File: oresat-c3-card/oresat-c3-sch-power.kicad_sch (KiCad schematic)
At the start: 68 parts, among them U31 LP2985AIM5-3.3, U34 TPS259621DDA, U35 TPS259620DDA, U36 LTC3624-5, U38 LP2985AIM5-3.3, U6 LTC3624-5

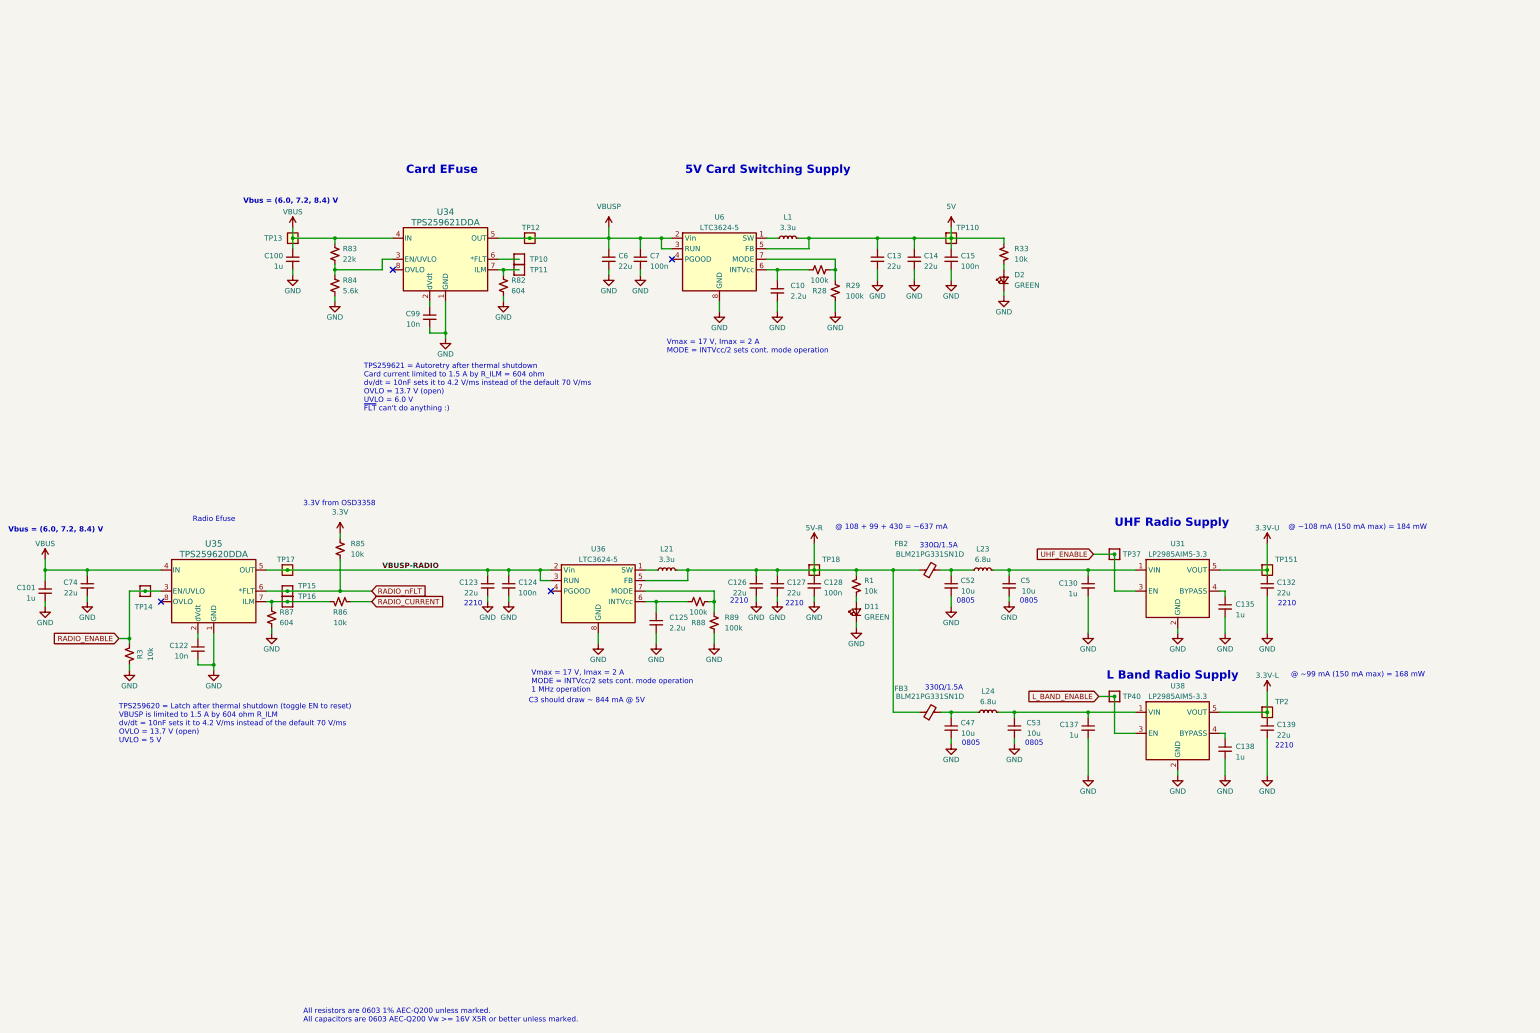
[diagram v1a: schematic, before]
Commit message: schematic changes following design review
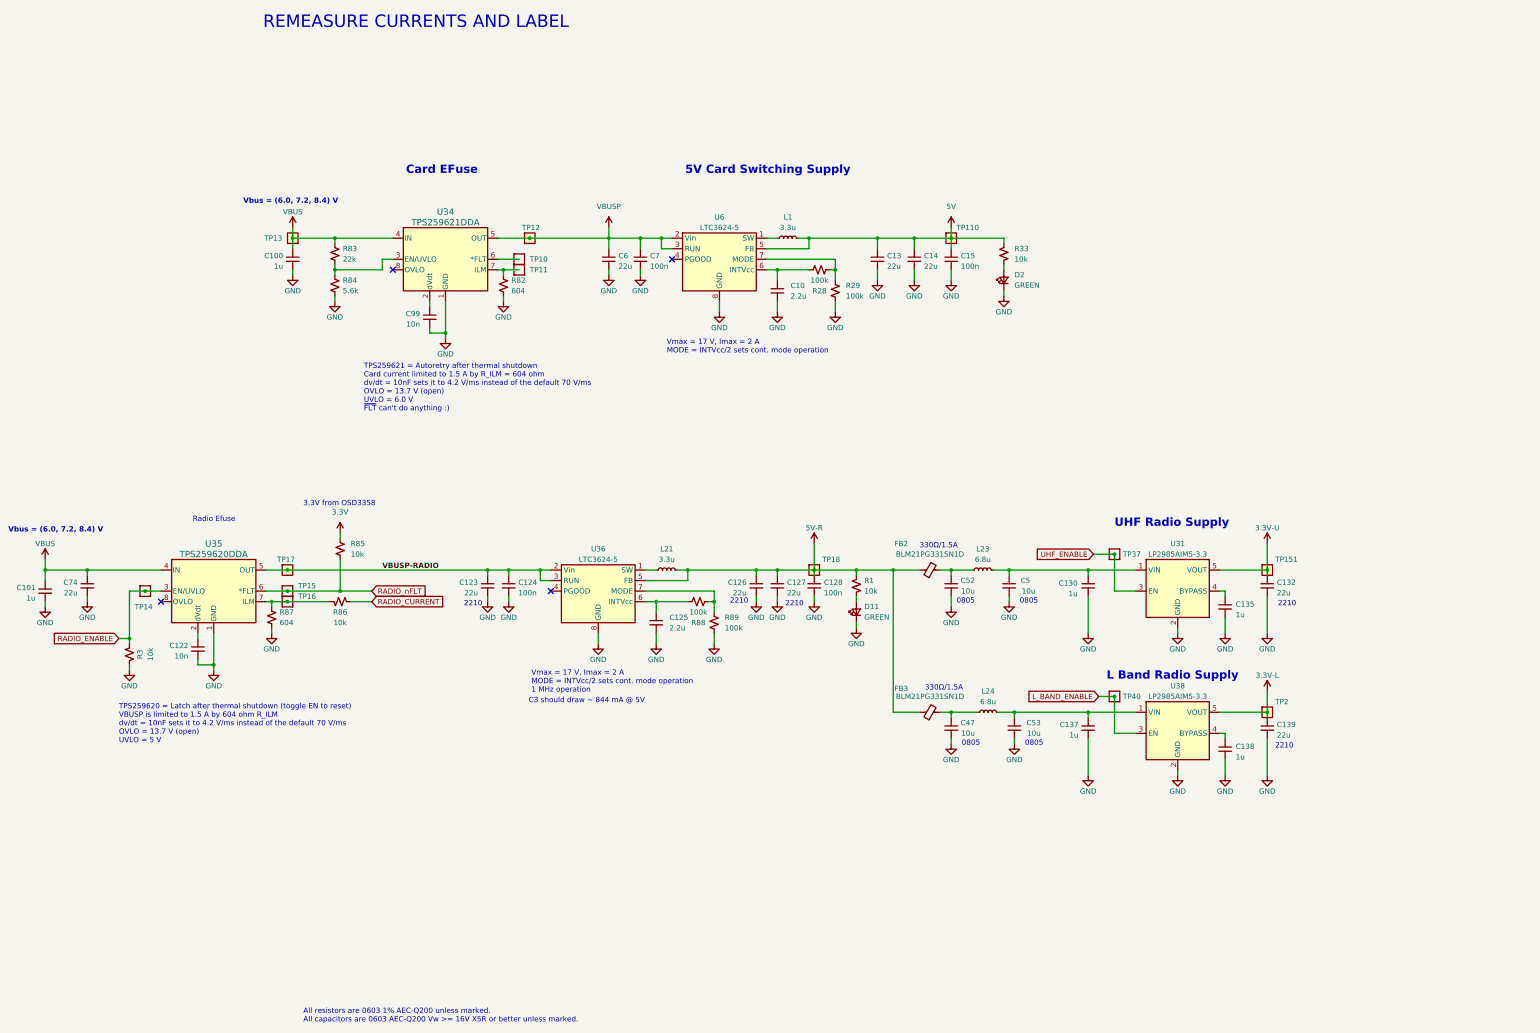
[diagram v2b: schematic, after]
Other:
- note added: "REMEASURE CURRENTS AND LABEL"
- note removed: "@ 108 + 99 + 430 = ~637 mA"
- note removed: "@ ~108 mA (150 mA max) = 184 mW"
- note removed: "@ ~99 mA (150 mA max) = 168 mW"
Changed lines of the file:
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@@
 		(company "Portland State Aerospace Society")
 	)
+	(text "REMEASURE CURRENTS AND LABEL"
+		(exclude_from_sim no)
+		(at 145.288 20.32 0)
+		(effects
+			(font
+				(size 3 3)
+			)
+		)
+	)
 	(text "330Ω/1.5A"
 		(exclude_from_sim no)
 		(at 266.7 147.32 0)
-		(effects
-			(font
-				(size 1.27 1.27)
-			)
-			(justify left bottom)
-		)
-	)
-	(text "@ ~99 mA (150 mA max) = 168 mW"
-		(exclude_from_sim no)
-		(at 356.235 178.435 0)
 		(effects
 			(font
@@
 		)
 	)
-	(text "@ 108 + 99 + 430 = ~637 mA"
-		(exclude_from_sim no)
-		(at 246.38 142.875 0)
-		(effects
-			(font
-				(size 1.27 1.27)
-			)
-			(justify left bottom)
-		)
-	)
 	(text "2210"
 		(exclude_from_sim no)
@@
 		(effects
 			(font
-				(size 1.27 1.27)
-			)
-			(justify left bottom)
-		)
-	)
-	(text "@ ~108 mA (150 mA max) = 184 mW"
-		(exclude_from_sim no)
-		(at 355.6 142.875 0)
-		(effects
-			(font

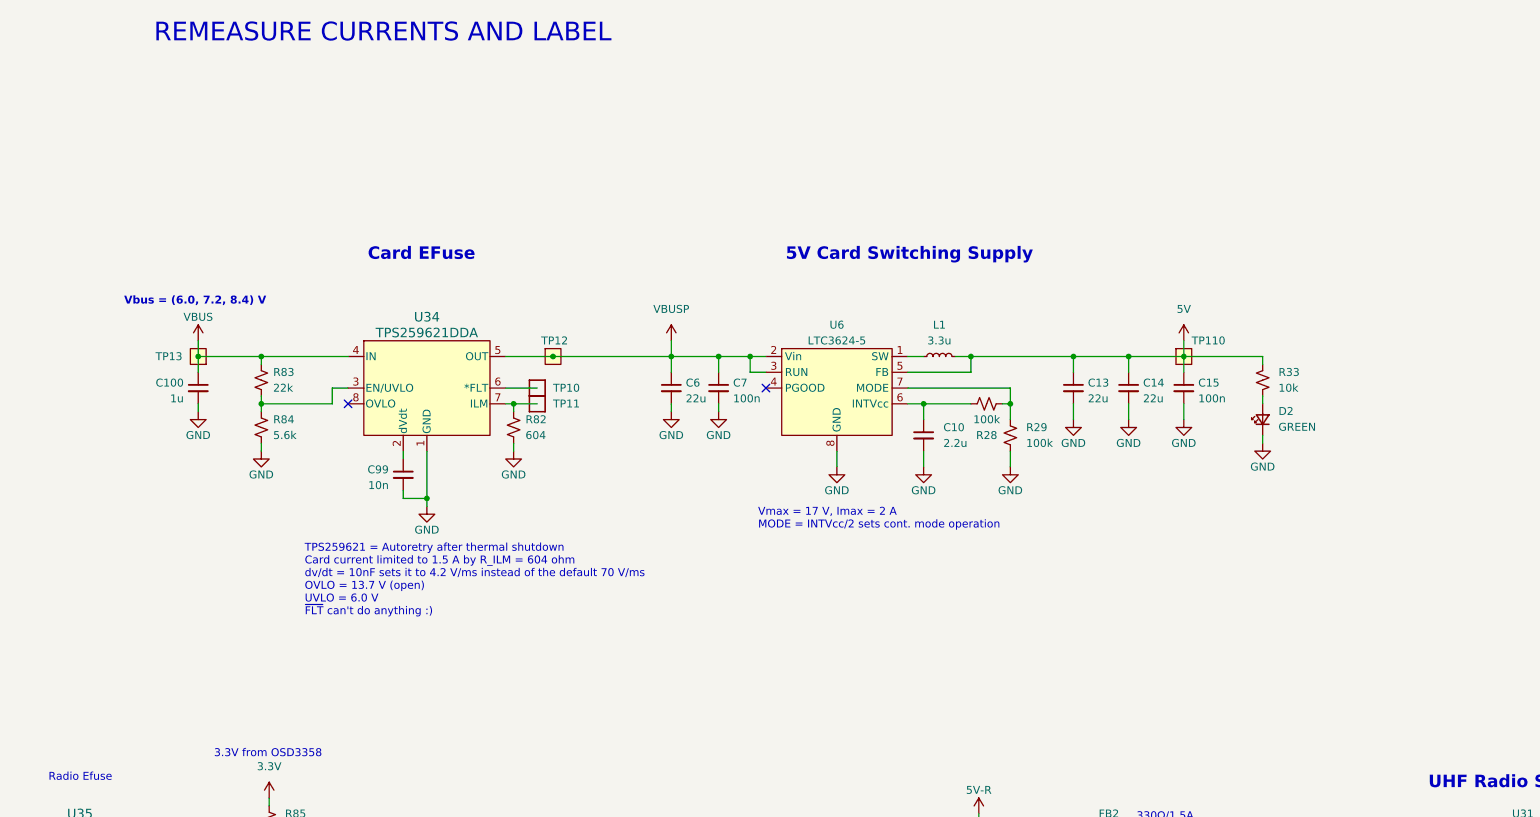
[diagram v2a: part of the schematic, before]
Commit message: Additional C3 design review changes and routing progress
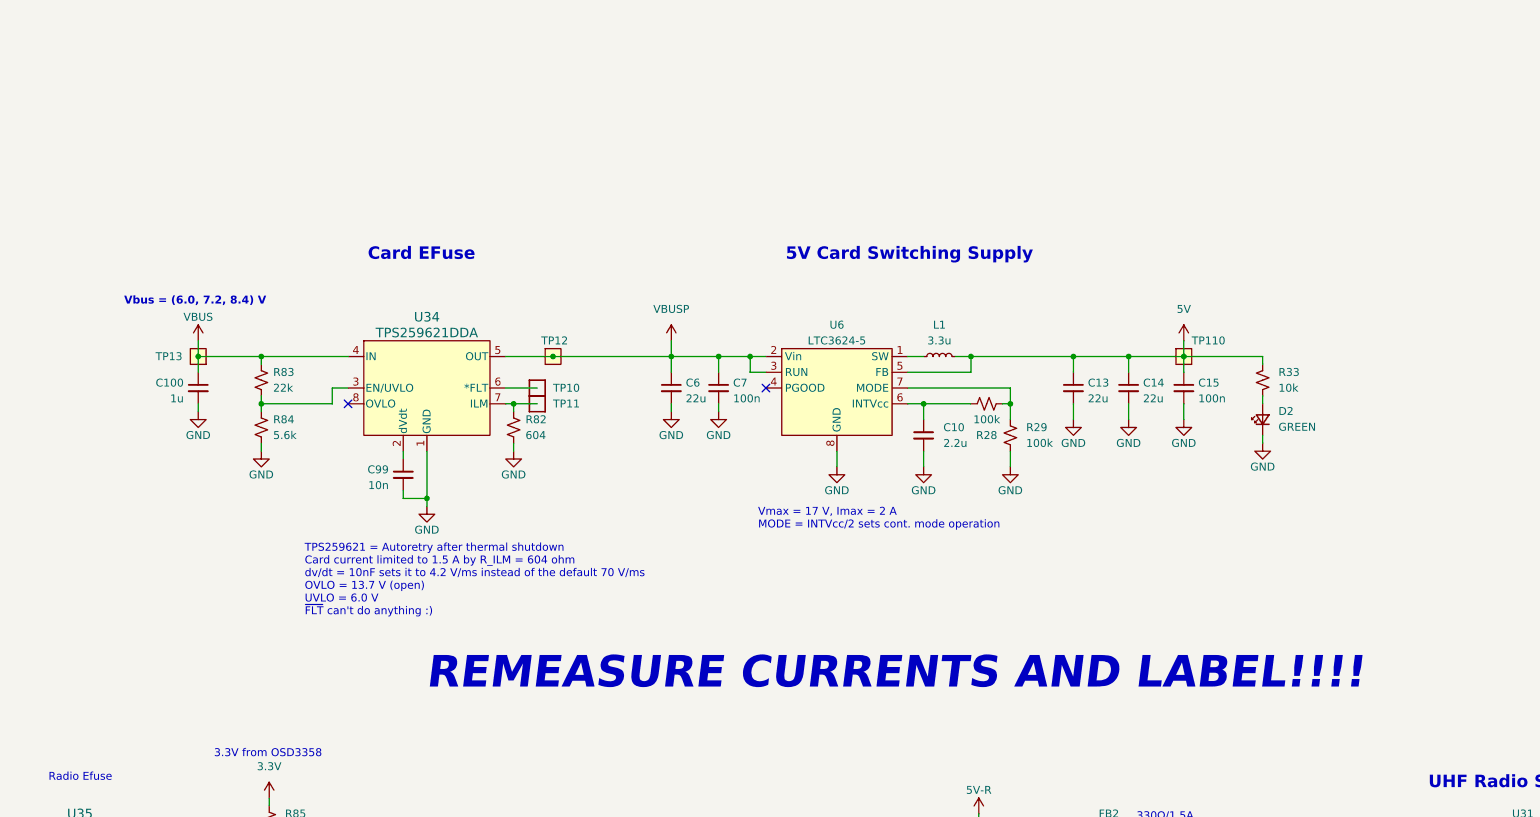
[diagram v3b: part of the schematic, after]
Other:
- note added: "REMEASURE CURRENTS AND LABEL!!!!"
- note removed: "REMEASURE CURRENTS AND LABEL"
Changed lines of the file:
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@@
 		(company "Portland State Aerospace Society")
 	)
-	(text "REMEASURE CURRENTS AND LABEL"
+	(text "REMEASURE CURRENTS AND LABEL!!!!"
 		(exclude_from_sim no)
-		(at 145.288 20.32 0)
+		(at 227.838 123.444 0)
 		(effects
 			(font
-				(size 3 3)
+				(face "KiCad Font")
+				(size 5.08 5.08)
+				(thickness 0.6)
+				(bold yes)
+				(italic yes)
+				(color 255 0 11 1)
 			)
 		)

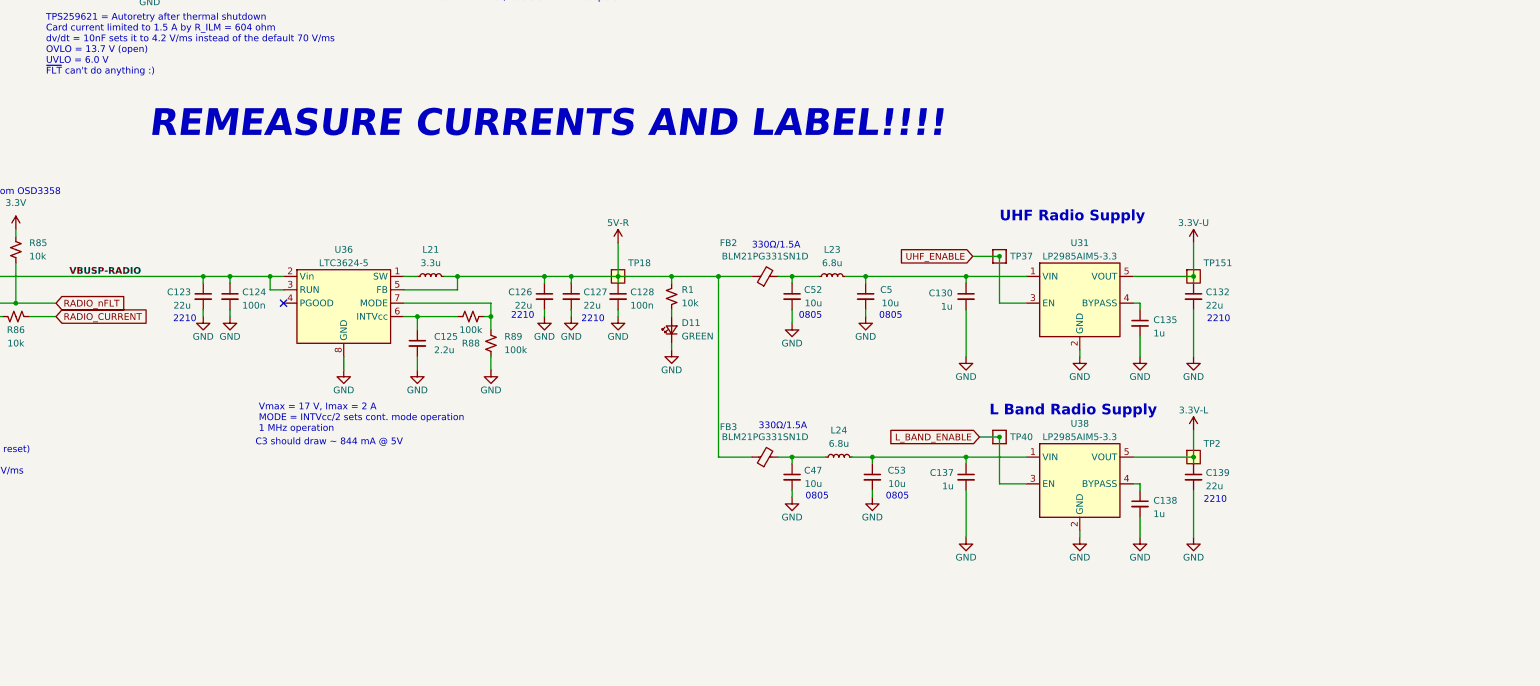
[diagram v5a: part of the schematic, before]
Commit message: Design review on C3 v7.0
Glenn and Andrew did a design review. Removed fiducials on back of board. Lots of schematic fixes, including
direction connection of TCXOs to AT86s, corrected LPF of CLKO from AT86 to the synth reference, fixed drive
levels both QPC switches in UHF radio, confirmed QPC directions, and some minor polishing.
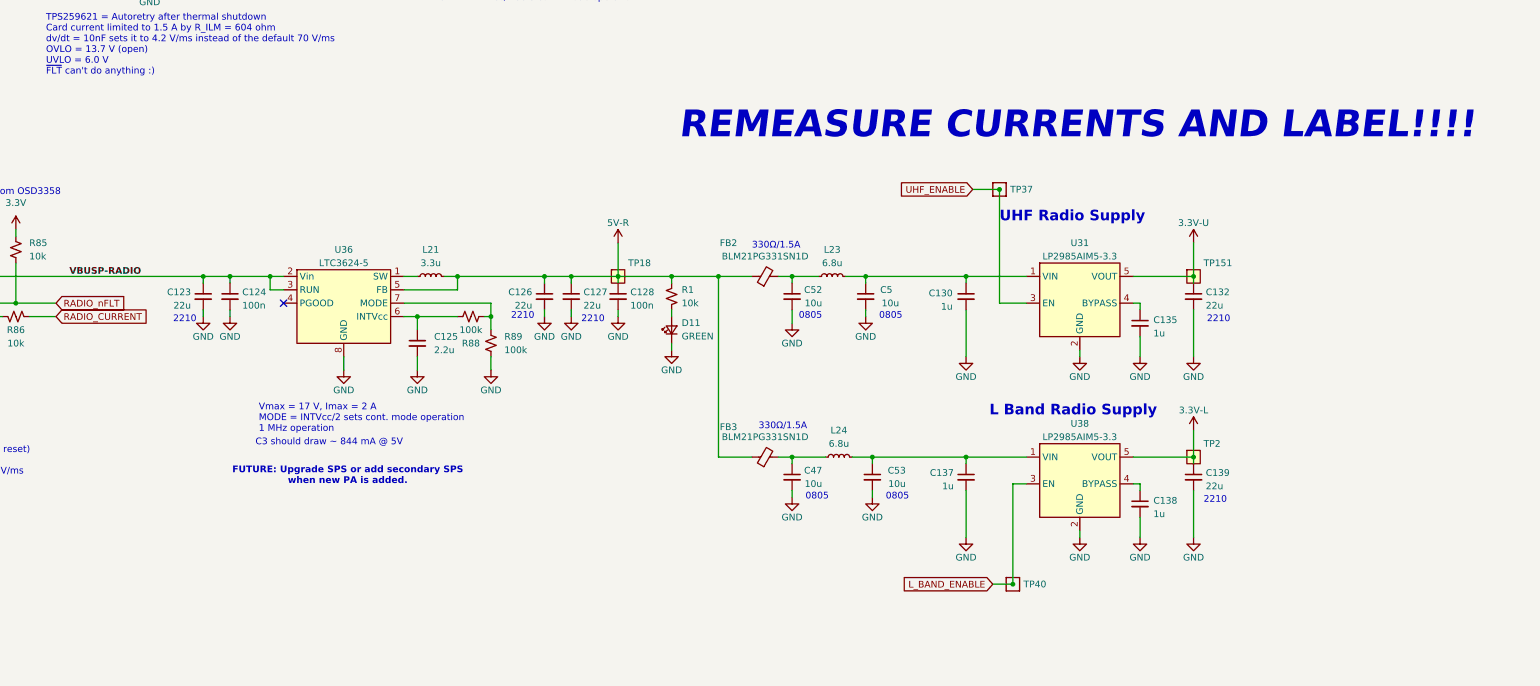
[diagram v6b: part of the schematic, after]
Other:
- note added: "FUTURE: Upgrade SPS or add secondary SPS when new PA is added."
- moved on the sheet: TP37, TP40
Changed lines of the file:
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@@
 	(text "REMEASURE CURRENTS AND LABEL!!!!"
 		(exclude_from_sim no)
-		(at 227.838 123.444 0)
+		(at 328.422 123.698 0)
 		(effects
 			(font
@@
 		)
 	)
+	(text "FUTURE: Upgrade SPS or add secondary SPS\nwhen new PA is added."
+		(exclude_from_sim no)
+		(at 189.992 190.246 0)
+		(effects
+			(font
+				(size 1.27 1.27)
+				(thickness 0.254)
+				(bold yes)
+			)
+		)
+	)
 	(text "330Ω/1.5A"
 		(exclude_from_sim no)
@@
 	)
 	(junction
-		(at 313.69 182.88)
+		(at 316.23 210.82)
 		(diameter 0)
 		(color 0 0 0 0)
@@
 	)
 	(junction
-		(at 313.69 148.59)
+		(at 313.69 135.89)
 		(diameter 0)
 		(color 0 0 0 0)
@@
 	(wire
 		(pts
-			(xy 309.88 182.88) (xy 313.69 182.88)
+			(xy 312.42 210.82) (xy 316.23 210.82)
 		)
 		(stroke
@@
 	(wire
 		(pts
-			(xy 313.69 191.77) (xy 313.69 182.88)
+			(xy 316.23 191.77) (xy 316.23 210.82)
 		)
 		(stroke
@@
 	(wire
 		(pts
-			(xy 308.61 148.59) (xy 313.69 148.59)
+			(xy 308.61 135.89) (xy 313.69 135.89)
 		)
 		(stroke
@@
 	(wire
 		(pts
-			(xy 313.69 148.59) (xy 313.69 157.48)
+			(xy 313.69 135.89) (xy 313.69 157.48)
 		)
 		(stroke
@@
 	(wire
 		(pts
-			(xy 313.69 191.77) (xy 318.77 191.77)
+			(xy 316.23 191.77) (xy 318.77 191.77)
 		)
 		(stroke
@@
 	(global_label "UHF_ENABLE"
 		(shape input)
-		(at 308.61 148.59 180)
+		(at 308.61 135.89 180)
 		(fields_autoplaced yes)
 		(effects
@@
 		)
 		(property "Intersheetrefs" "${INTERSHEET_REFS}"
-			(at 293.8924 148.59 0)
+			(at 293.8924 135.89 0)
 			(effects
 				(font
@@
 	(global_label "L_BAND_ENABLE"
 		(shape input)
-		(at 309.88 182.88 180)
+		(at 312.42 210.82 180)
 		(fields_autoplaced yes)
 		(effects
@@
 		)
 		(property "Intersheetrefs" "${INTERSHEET_REFS}"
-			(at 291.9572 182.88 0)
+			(at 294.4972 210.82 0)
 			(effects
 				(font
@@
 	(symbol
 		(lib_id "oresat-misc:Test-Point-1mm-round")
-		(at 313.69 182.88 180)
+		(at 316.23 210.82 180)
 		(unit 1)
 		(exclude_from_sim yes)
@@
 		(dnp no)
 		(property "Reference" "TP40"
-			(at 320.04 182.88 0)
+			(at 322.58 210.82 0)
 			(effects
 				(font
@@
 		)
 		(property "Value" "Test-Point"
-			(at 313.69 185.42 0)
+			(at 316.23 213.36 0)
 			(effects
 				(font
@@
 		)
 		(property "Footprint" "oresat-misc:TestPoint_Pad_D1.0mm"
-			(at 313.69 193.04 0)
+			(at 316.23 220.98 0)
 			(effects
 				(font
@@
 		)
 		(property "Datasheet" ""
-			(at 313.69 182.88 0)
+			(at 316.23 210.82 0)
 			(effects
 				(font
@@
 		)
 		(property "Description" "1mm round SMT test point"
-			(at 313.69 182.88 0)
+			(at 316.23 210.82 0)
 			(effects
 				(font
@@
 	(symbol
 		(lib_id "oresat-misc:Test-Point-1mm-round")
-		(at 313.69 148.59 180)
+		(at 313.69 135.89 180)
 		(unit 1)
 		(exclude_from_sim yes)
@@
 		(dnp no)
 		(property "Reference" "TP37"
-			(at 320.04 148.59 0)
+			(at 320.04 135.89 0)
 			(effects
 				(font
@@
 		)
 		(property "Value" "Test-Point"
-			(at 313.69 151.13 0)
+			(at 313.69 138.43 0)
 			(effects
 				(font
@@
 		)
 		(property "Footprint" "oresat-misc:TestPoint_Pad_D1.0mm"
-			(at 313.69 158.75 0)
+			(at 313.69 146.05 0)
 			(effects
 				(font
@@
 		)
 		(property "Datasheet" ""
-			(at 313.69 148.59 0)
+			(at 313.69 135.89 0)
 			(effects
 				(font
@@
 		)
 		(property "Description" "1mm round SMT test point"
-			(at 313.69 148.59 0)
+			(at 313.69 135.89 0)
 			(effects
 				(font
